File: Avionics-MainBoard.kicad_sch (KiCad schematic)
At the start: 0 parts

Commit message: temp
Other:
- sheet Connectors ports: added Jetson_CLK, Jetson_CSn, Jetson_MISO, Jetson_MOSI; removed MCU_RX_JETSON, MCU_TX_JETSON
- sheet GPS Power ports: added SCL, SDA; removed SCL_BUS, SDA_BUS
- sheet LoRa Power ports: added SCL, SDA; removed SCL_BUS, SDA_BUS
- sheet MCU_IO ports: added Jetson_CSn, SPI0_CLK, SPI0_MISO, SPI0_MOSI, SPI1_CLK, SPI1_MISO, SPI1_MOSI, UART0_RX, UART0_TX, UART1_RX, UART1_TX; removed LoRa_CLK, LoRa_MISO, LoRa_MOSI, MCU_RX_GPS, MCU_RX_Jetson, MCU_TX_GPS, MCU_TX_Jetson, SD_CLK, SD_MISO, SD_MOSI
- sheet Main Power ports: added SCL, SDA; removed SCL_BUS, SDA_BUS

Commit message: v1 done
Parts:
- added H1, H2, H3, H4: MountingHole_Pad, MountingHole:MountingHole_3.2mm_M3_DIN965_Pad_TopBottom, symbol Mechanical:MountingHole_Pad
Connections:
- new net GND: H1.1, H2.1, H3.1, H4.1
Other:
- added sheet RS485 (RS485.kicad_sch)
- sheet Connectors ports: added RX+, RX-, TX+, TX-; removed Battery_ALERT, Jetson_EN
- sheet MCU_IO ports: added RS485_RX_EN, RS485_TX_EN; removed Battery_ALERT, Jetson_EN

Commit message: Updated i2c device addresses and mcu caps
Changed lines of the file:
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@@
 	(sheet
 		(at 46.99 22.225)
-		(size 25.4 225.425)
+		(size 25.4 229.235)
 		(fields_autoplaced yes)
 		(stroke
@@
 		)
 		(property "Sheetfile" "MCU_IO.kicad_sch"
-			(at 46.99 248.2346 0)
+			(at 46.99 252.0446 0)
 			(effects
 				(font
@@
 		(pin "IMU_INTn" input
 			(at 72.39 198.12 0)
-			(effects
-				(font
-					(size 1.27 1.27)
-				)
-				(justify right)
-			)
-		)
-		(pin "UART0_TX" output
-			(at 72.39 113.03 0)
-			(effects
-				(font
-					(size 1.27 1.27)
-				)
-				(justify right)
-			)
-		)
-		(pin "UART0_RX" input
-			(at 72.39 116.84 0)
 			(effects
 				(font
@@
 	(sheet
 		(at 97.79 209.55)
-		(size 25.4 38.1)
+		(size 25.4 41.91)
 		(fields_autoplaced yes)
 		(stroke
@@
 		)
 		(property "Sheetfile" "Connectors.kicad_sch"
-			(at 97.79 248.2346 0)
-			(effects
-				(font
+			(at 97.79 252.0446 0)
+			(effects
+				(font

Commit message: Added extra connector
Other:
- sheet Connectors ports: added Battery_ALERT, Jetson_EN; removed none
- sheet LoRa Power ports: added none; removed LoRa_DIO1, LoRa_DIO2
- sheet MCU_IO ports: added Battery_ALERT, Jetson_EN; removed LoRa_DIO1, LoRa_DIO2
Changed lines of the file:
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@@
-	(wire
-		(pts
-			(xy 72.39 74.93) (xy 97.79 74.93)
-		)
-		(stroke
-			(width 0)
-			(type default)
-		)
-	)
 	(wire
 		(pts
@@
 	(wire
 		(pts
-			(xy 72.39 77.47) (xy 97.79 77.47)
-		)
-		(stroke
-			(width 0)
-			(type default)
-		)
-	)
-	(wire
-		(pts
 			(xy 72.39 29.21) (xy 97.79 29.21)
 		)
@@
 	(wire
 		(pts
+			(xy 72.39 248.92) (xy 97.79 248.92)
+		)
+		(stroke
+			(width 0)
+			(type default)
+		)
+	)
+	(wire
+		(pts
 			(xy 127 31.75) (xy 127 231.14)
 		)
@@
 			(type default)
 			(color 255 153 0 1)
+		)
+	)
+	(wire
+		(pts
+			(xy 72.39 238.76) (xy 97.79 238.76)
+		)
+		(stroke
+			(width 0)
+			(type default)
 		)
 	)
@@
 			)
 		)
-		(pin "LoRa_DIO2" bidirectional
-			(at 72.39 74.93 0)
-			(effects
-				(font
-					(size 1.27 1.27)
-				)
-				(justify right)
-			)
-		)
-		(pin "LoRa_DIO1" bidirectional
-			(at 72.39 77.47 0)
-			(effects
-				(font
-					(size 1.27 1.27)
-				)
-				(justify right)
-			)
-		)
 		(pin "LoRa_RX_EN" output
 			(at 72.39 90.17 0)
@@
 		(pin "RS485_RX_EN" output
 			(at 72.39 31.75 0)
+			(effects
+				(font
+					(size 1.27 1.27)
+				)
+				(justify right)
+			)
+		)
+		(pin "Jetson_EN" output
+			(at 72.39 238.76 0)
+			(effects
+				(font
+					(size 1.27 1.27)
+				)
+				(justify right)
+			)
+		)
+		(pin "Battery_ALERT" input
+			(at 72.39 248.92 0)
 			(effects
 				(font
@@
 			)
 		)
+		(pin "Battery_ALERT" output
+			(at 97.79 248.92 180)
+			(effects
+				(font
+					(size 1.27 1.27)
+				)
+				(justify left)
+			)
+		)
+		(pin "Jetson_EN" input
+			(at 97.79 238.76 180)
+			(effects
+				(font
+					(size 1.27 1.27)
+				)
+				(justify left)
+			)
+		)
 		(instances
 			(project "Avionics-MainBoard"
@@
 			(effects
 				(font
-					(size 1.27 1.27)
-				)
-				(justify left)
-			)
-		)
-		(pin "LoRa_DIO1" bidirectional
-			(at 97.79 77.47 180)
-			(effects
-				(font
-					(size 1.27 1.27)
-				)
-				(justify left)
-			)
-		)
-		(pin "LoRa_DIO2" bidirectional
-			(at 97.79 74.93 180)
-			(effects
-				(font

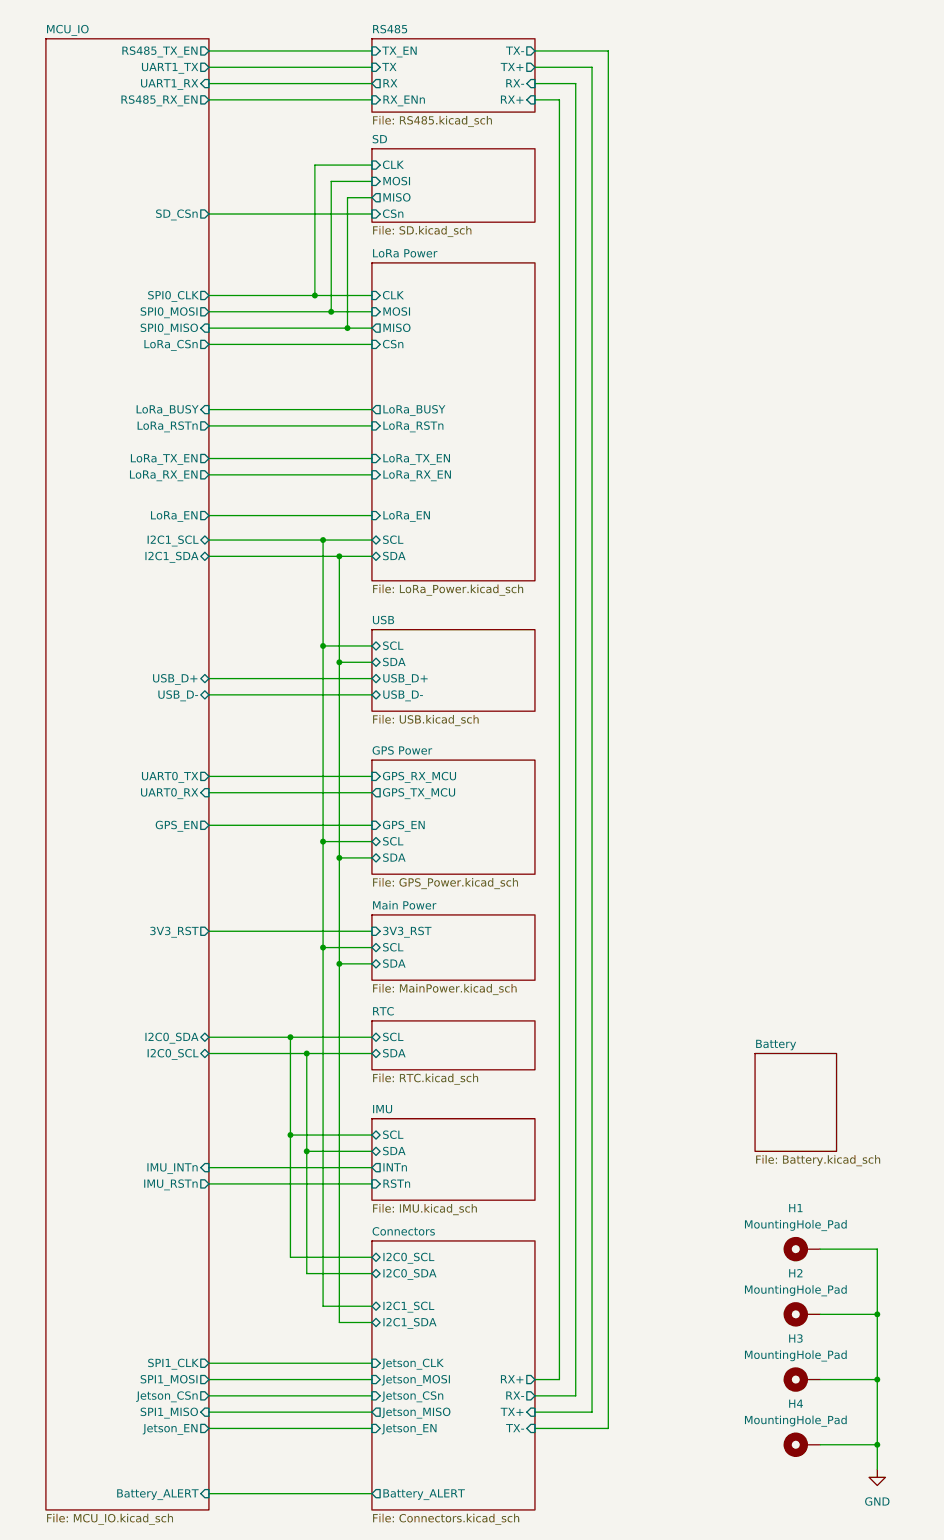
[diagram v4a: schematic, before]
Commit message: Fixed schematic bugs and corresponding layout modifications
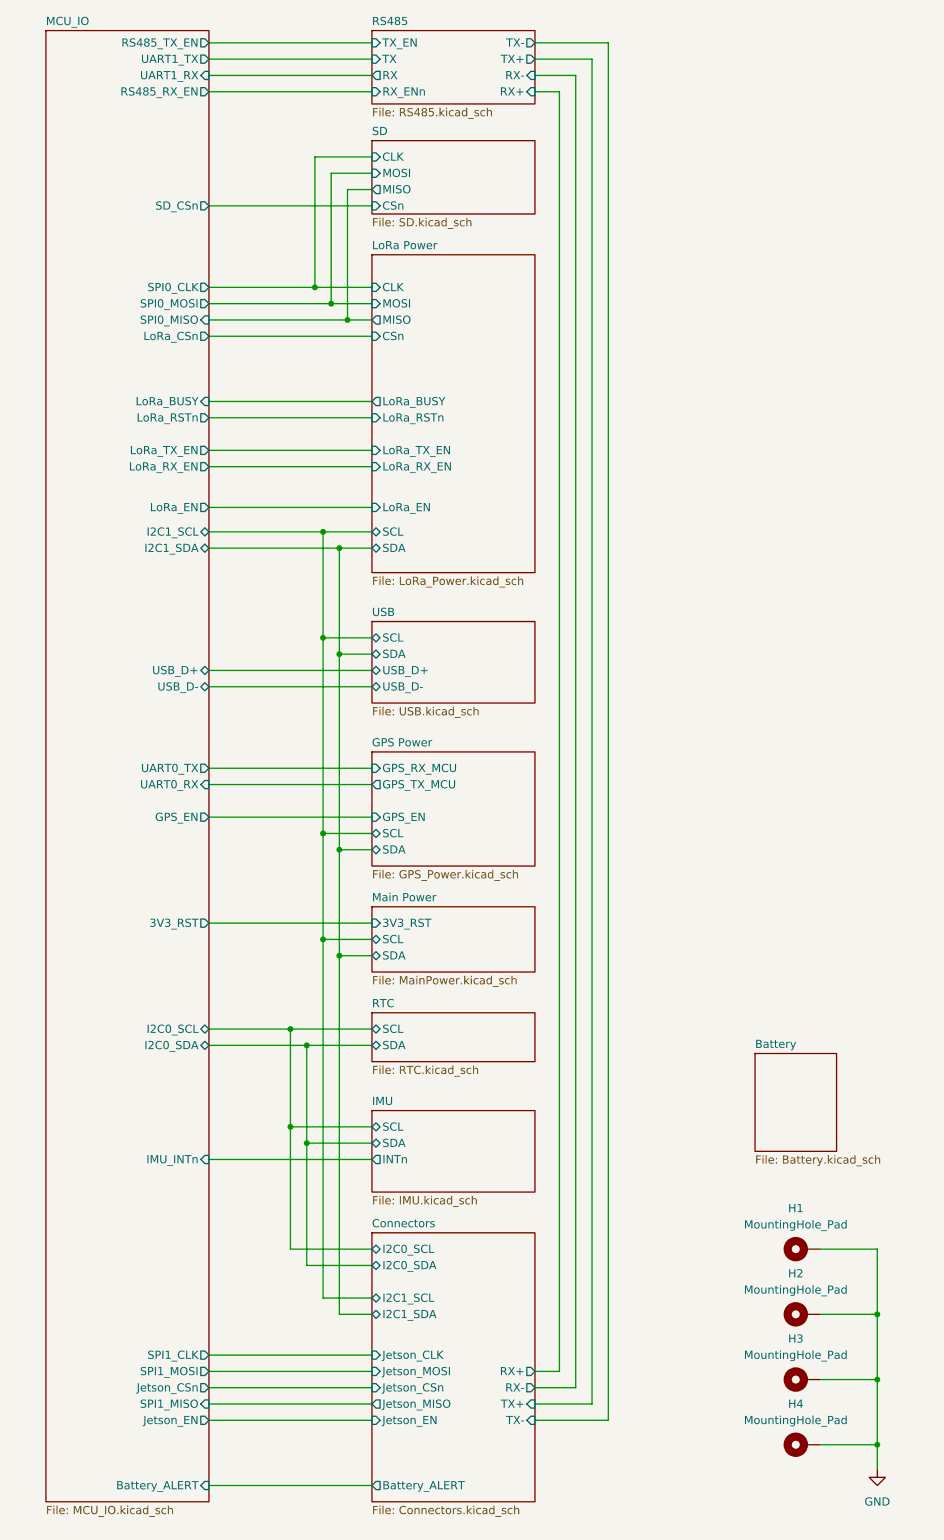
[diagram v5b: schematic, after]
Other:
- sheet IMU ports: added none; removed RSTn
- sheet MCU_IO ports: added none; removed IMU_RSTn

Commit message: Added better protection to SD card, Jetson IO, and added address breakouts to power monitors
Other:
- sheet GPS Power ports: added none; removed GPS_EN
- sheet LoRa Power ports: added LoRa_INT; removed none
- sheet MCU_IO ports: added LoRa_INT; removed GPS_EN
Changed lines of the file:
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@@
-	(wire
-		(pts
-			(xy 72.39 143.51) (xy 97.79 143.51)
-		)
-		(stroke
-			(width 0)
-			(type default)
-		)
-	)
 	(wire
 		(pts
@@
 		(pts
 			(xy 127 30.48) (xy 127 229.87)
+		)
+		(stroke
+			(width 0)
+			(type default)
+		)
+	)
+	(wire
+		(pts
+			(xy 72.39 92.71) (xy 97.79 92.71)
 		)
 		(stroke
@@
 			)
 		)
-		(pin "GPS_EN" input
-			(at 97.79 143.51 180)
-			(effects
-				(font
-					(size 1.27 1.27)
-				)
-				(justify left)
-			)
-		)
 		(pin "GPS_TX_MCU" output
 			(at 97.79 138.43 180)
@@
 			)
 		)
-		(pin "GPS_EN" output
-			(at 72.39 143.51 0)
-			(effects
-				(font
-					(size 1.27 1.27)
-				)
-				(justify right)
-			)
-		)
 		(pin "LoRa_CSn" output
 			(at 72.39 68.58 0)
@@
 		(pin "Battery_ALERT" input
 			(at 72.39 247.65 0)
+			(effects
+				(font
+					(size 1.27 1.27)
+				)
+				(justify right)
+			)
+		)
+		(pin "LoRa_INT" input
+			(at 72.39 92.71 0)
 			(effects
 				(font
@@
 			(effects
 				(font
+					(size 1.27 1.27)
+				)
+				(justify left)
+			)
+		)
+		(pin "LoRa_INT" output
+			(at 97.79 92.71 180)
+			(effects
+				(font

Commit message: Updated version to v2.1
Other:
- company: (none) -> Carnegie Mellon University
- title: (none) -> Argus Mainboard
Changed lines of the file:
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@@
 	(generator_version "8.0")
 	(paper "A4" portrait)
+	(title_block
+		(title "Argus Mainboard")
+		(date "2024-11-19")
+		(rev "v2.1")
+		(company "Carnegie Mellon University")
+		(comment 1 "M. Holliday")
+		(comment 2 "N. Khera")
+		(comment 3 "V. Rajesh")
+	)
 	(junction
 		(at 92.71 101.6)

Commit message: v3 partial schematic updates
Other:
- sheet GPS Power renamed GPS
- sheet LoRa Power renamed LoRa
- removed sheet RS485
- added sheet Payload (Payload.kicad_sch)
- sheet Connectors ports: added Jetson_RX, Jetson_TX; removed Jetson_CLK, Jetson_CSn, Jetson_MISO, Jetson_MOSI, RX+, RX-, TX+, TX-
- sheet GPS: file GPS_Power.kicad_sch -> GPS.kicad_sch
- sheet GPS ports: added GPS_EN, GPS_FLT; removed SCL, SDA
- sheet IMU ports: added none; removed INTn
- sheet LoRa: file LoRa_Power.kicad_sch -> LoRa.kicad_sch
- sheet MCU_IO ports: added none; removed IMU_INTn, Jetson_CSn, RS485_RX_EN, RS485_TX_EN
- sheet Main Power ports: added 3V3_M_RST, 3V3_P_EN; removed 3V3_RST
- sheet USB ports: added none; removed SCL, SDA
